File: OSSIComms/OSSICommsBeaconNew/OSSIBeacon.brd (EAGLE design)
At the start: 82 x 82 mm, 21 parts, among them U10 MAX6369, U12 TPS73233, U3 MAX890L, U4 OPA2347, U7 TPS3838, X2 DF13-10PA

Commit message: OSSI New Beacon Board Circuit 90% done
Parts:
- added C10, C11, C14, C15, C16, C22, C25, C32, C4, C5, C6, C8, C9: (no value), OSSI:C0603(1608)
- added C17, C18: 12.5pF, OSSI:C0603(1608)
- added C2, C24, C29, C31: 100nF, OSSI:C0603(1608)
- added C23: 1uF, OSSI:C0603(1608)
- added C26: 1uF,0805, OSSI:C0805(2012)
- added C27, C28, C76: 10nF, OSSI:C0603(1608)
- added C3: 1uF, 0805, OSSI:C0805(2012)
- added C30: 10uF,1210, OSSI:C1210-GCM32
- added C62: 22nF, OSSI:C0603(1608)
- added C7: 1uF 0805, OSSI:C0805(2012)
- added C77: 22pF, OSSI:C0603(1608)
- added F1: LFCN-160, OSSI:LFCN
- added L1, L2: 470nH, 1008 size, OSSI:L1008(2520)
- added L10: 10nH, OSSI:L0603(1608)
- added L3, L4: (no value), OSSI:L0603(1608)
- added LED1: (no value), SparkFun:LED-0603
- added Q2: NX-3215, OSSI:NX-3215
- added R1, R12, R34: 100k, OSSI:R0603(1608)
- added R13: 1.6k, OSSI:R0603(1608)
- added R16: 4.7k, OSSI:R0603(1608)
- added R2, R3: (no value), OSSI:R0603(1608)
- added R25: 3.6k, OSSI:R0603(1608)
- added R33: 1k, OSSI:R0603(1608)
- added R4: 0, OSSI:R0603(1608)
- added R63, R67: 250, OSSI:R0603(1608)
- added R68, R71: 10k, OSSI:R0603(1608)
- added TCXO1: 19.2MHz, OSSI:TCXO_M532
- added TR3: FDV301N, OSSI:SOT23
- added U1: MSP430F2132, OSSI:PW28
- added U2: ADF7012, OSSI:TSSOP24
- added U5: ADL5530, OSSI:LFCSP8_CP
- added U6: MAX890L, OSSI:SO8
- added X1: RFCON-MCX-R/A, OSSI:MCX-R/A
- added X5: JTAG10PINMINI-H, OSSI:M50-3200545
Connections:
- new net BEACON_CE: U1.18, U2.14
- new net BEACON_DATA: U1.24, U2.4
- new net BEACON_MUXOUT: U1.22, U2.6
- new net BEACON_RFOUT: C25.2, C27.1, L4.2
- new net BEACON_SCLK: U1.21, U2.11
- new net BEACON_SDATA: U1.20, U2.12
- new net BEACON_SLE: U1.19, U2.13
- new net BEACON_TCXO: C77.2, U2.8
- new net BEACON_TXCLK: U1.23, U2.5
- new net N$1: R33.1, U1.14
- new net N$10: R67.2, U1.13
- new net N$11: R22.1
- new net N$12: U1.10, U10.1
- new net N$13: U1.11
- new net N$14: L10.1, U2.16
- new net N$15: L10.2, U2.15
- new net N$16: C62.1, C7.2, U2.24
- new net N$17: C62.2, U2.17
- new net N$18: R25.2, U2.23
- new net N$19: C23.1, R12.1, TR3.3, U6.3
- new net N$2: U1.27, X5.3
- new net N$20: C5.1, R3.1
- new net N$21: R13.2, U6.5
- new net N$23: C15.2, L1.P$2, U2.20
- new net N$24: C4.1, R2.1, U2.18
- new net N$25: C3.2, U2.2
- new net N$26: C5.2, C6.2, R2.2, U2.3
- new net N$27: C8.1, C9.1, L1.P$1, R4.2, U2.21
- new net N$28: C27.2, U5.2
- new net N$29: C15.1, C16.2, L3.1
- new net N$3: U1.26, X5.5
- new net N$30: C28.1, L2.P$2, U5.7
- new net N$31: R16.1, X5.10
- new net N$34: C28.2, F1.1
- new net N$35: C32.1, F1.3
- new net N$36: C22.2, L3.2, L4.1
- new net N$37: C32.2, X1.1
- new net N$4: U1.25, X5.7
- new net N$5: C17.1, Q2.2, U1.5
- new net N$6: C18.1, Q2.1, U1.6
- new net N$69: C77.1, TCXO1.3
- new net N$7: LED1.A, R33.2
- new net N$8: U1.28, X5.1
- new net N$9: R63.2, U1.12
- new net PA_-FAULT: R34.1, U1.3, U6.8
- new net PA_ON: R1.2, TR3.1, U1.17
- new net RXD: U1.16
- new net TXD: U1.15
- new net VCCRF: C10.1, C11.1, C14.1, C76.1, R4.1, TCXO1.4, U2.1
- net 3.3VBEACON: now also C2.1, R34.2, R68.2, R71.2, U1.2, X5.4
- net ADC0: now also U1.8
- net ADC1: now also U1.9
- net GND: now also C10.2, C11.2, C14.2, C16.1, C17.2, C18.2, C2.2, C22.1, C23.2, C24.2, C25.1, C26.2, C29.2, C3.1, C30.P$2, C31.2, C4.2, C6.1, C7.1, C76.2, C8.2, C9.2, F1.2, F1.4, LED1.C, R1.1, R13.1, R25.1, R3.2, TCXO1.1, TCXO1.2, TR3.2, U1.4, U2.19, U2.22, U2.7, U5.1, U5.3, U5.4, U5.5, U5.6, U5.8, U6.4, X1.2, X1.3, X1.4, X1.5, X5.9
- net I2CSEC_SCL: now also R67.1, R71.1
- net I2CSEC_SDA: now also R63.1, R68.1
- net RESETBEACON: now also R16.2, U1.7
- net VBEACON_PA: now also C24.1, C26.1, C29.1, C30.P$1, C31.1, L2.P$1, U6.6, U6.7; no longer R22.1
- net VBUS: now also R12.2, U6.1, U6.2

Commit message: New Beacon board updating
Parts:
- added H1, H2, H3, H4: MOUNT-PAD-ROUND3.2, OSSI:3.2-PAD-ROUND
- moved C32 495.0 mm to (67.6, 66.4)
- moved C31 485.7 mm to (55.9, 73.7)
- moved F1 483.7 mm to (62.5, 66.4)
- moved C29 476.8 mm to (55.9, 71.1)
- moved C28 466.1 mm to (58.1, 66.4)
- moved C27 458.6 mm to (47.6, 66.4)
- moved C25 451.8 mm to (45.7, 63.5), turned to 90 degrees
- moved C22 447.7 mm to (43.2, 63.5), turned to 90 degrees
- moved C16 443.7 mm to (40.3, 63.5), turned to 90 degrees
- moved L4 443.1 mm to (44.5, 66.4)
- moved L3 436.5 mm to (41.3, 66.4)
- moved L2 432.3 mm to (54.6, 67.3)
- moved C15 417.2 mm to (37.5, 66.4), turned to 180 degrees
- moved L1 411.2 mm to (33.0, 67.3)
- moved C14 401.8 mm to (26.0, 70.8), turned to 90 degrees
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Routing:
- net 3.3VBEACON: track 0.00 -> 118.2 mm
- net VBEACON_PA: track 0.00 -> 110.7 mm
- net VBUS: track 0.00 -> 72.1 mm
- net BEACON_DATA: track 0.00 -> 60.2 mm
- net BEACON_TXCLK: track 0.00 -> 57.7 mm
- net BEACON_MUXOUT: track 0.00 -> 56.4 mm
- net BEACON_OFF: track 0.00 -> 38.5 mm
- net I2CSEC_SDA: track 0.00 -> 30.1 mm
- net BEACON_-FAULT: track 0.00 -> 30.0 mm
- net BEACON_SCLK: track 0.00 -> 29.6 mm
- net BEACON_SDATA: track 0.00 -> 28.0 mm
- net N$666: track 0.00 -> 26.9 mm
- net I2CSEC_SCL: track 0.00 -> 26.5 mm
- net ADC1: track 0.00 -> 24.0 mm
- net BEACON_WDT_RST: track 0.00 -> 22.7 mm, vias 0 -> 2
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- removed copper zone on layer 1, net GND
- removed copper zone on layer 16, net GND
- removed copper zone on layer 1, net N$34
- removed copper zone on layer 16, net N$34

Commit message: OSSI New Beacon Almost done
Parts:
- added C33, C36: 10pF, OSSI:C0603(1608)
- added C37: 10nF, OSSI:C0603(1608)
- added C38: 100nF, OSSI:C0603(1608)
- added L11: 0 Ohm, OSSI:L0805(2012)
- added Q1: CX5032SB, OSSI:CX5032
- added U$1: OSSILOGORECT, OSSI:OSSILOGORECT1005
- added X3: MOLEX-22-05-7035, OSSI:22-05-7035
- moved X5 74.9 mm to (4.21, 33.7), turned to 270 degrees
- moved R16 63.2 mm to (9.21, 31.1), turned to 0 degrees
- moved R33 58.4 mm to (10.2, 10.6)
- moved LED1 58.3 mm to (10.2, 7.78)
- moved R12 33.8 mm to (39.1, 10.5), turned to 270 degrees
- moved U6 32.8 mm to (34.3, 10.2), turned to 90 degrees
- moved TR3 32.5 mm to (41.9, 12.1)
- moved C24 32.3 mm to (29.2, 11.7), turned to 90 degrees
- moved R1 31.6 mm to (44.8, 12.1)
- moved C23 29.2 mm to (39.1, 13.3), turned to 90 degrees
- moved U10 24.2 mm to (14.0, 32.4), turned to 270 degrees
- moved R13 24.0 mm to (31.8, 14.0), turned to 180 degrees
- moved C1 20.7 mm to (17.1, 32.4), turned to 90 degrees
- moved R34 16.9 mm to (21.6, 38.1), turned to 270 degrees
- moved U1 15.5 mm to (16.5, 41.9), turned to 90 degrees
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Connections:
- removed net I2CSEC_SCL: R67.1, R71.1, X2.4
- removed net I2CSEC_SDA: R63.1, R68.1, X2.5
- removed net N$11: R22.1
- new net BEACON_ADCIN: R22.1, X2.5
- new net BEACON_CWCONTROL: X2.4
- new net N$41: C33.1, Q1.3, U2.9
- net 3.3VBEACON: now also C37.1, L11.1
- net BEACON_SCL: now also R67.1, R71.1
- net BEACON_SDA: now also R63.1, R68.1
- net BEACON_TCXO: now also C36.1, Q1.1
- net GND: now also C33.2, C36.2, C37.2, C38.2, Q1.2, Q1.4, X3.1
- net N$1: now also U1.11; no longer U1.14
- net N$13: now also U1.14; no longer U1.11
- net RXD: now also X3.3
- net TXD: now also X3.2
- net VCCRF: now also C38.1, L11.2
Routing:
- net GND: track 9.76 -> 133.7 mm, vias 0 -> 137
- net VCCRF: track 5.59 -> 112.2 mm, vias 0 -> 2
- net PA_ON: track 10.4 -> 95.4 mm, vias 0 -> 2
- net PA_-FAULT: track 2.53 -> 73.1 mm, vias 0 -> 2
- net TXD: track 0.00 -> 52.6 mm, vias 0 -> 1
- net RXD: track 0.00 -> 51.2 mm, vias 0 -> 1
- net VBEACON_PA: track 110.7 -> 152.5 mm
- net BEACON_ADCIN: track 0.00 -> 39.5 mm, vias 0 -> 2
- net BEACON_SDA: track 0.00 -> 34.2 mm, vias 0 -> 2
- net BEACON_SCL: track 0.00 -> 32.7 mm, vias 0 -> 2
- net I2CSEC_SDA: track 30.1 -> 0.00 mm
- net I2CSEC_SCL: track 26.5 -> 0.00 mm
- net RESETBEACON: track 11.9 -> 36.7 mm, vias 0 -> 2
- net N$666: track 26.9 -> 8.65 mm
- net BEACON_WDT_RST: track 22.7 -> 4.72 mm, vias 2 -> 0
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- added copper zone on layer 1, net GND
- added copper zone on layer 16, net GND
- added copper zone on layer 1, net N$38
- added copper zone on layer 16, net N$38

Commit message: OSSI New Beacon layout done
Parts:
- added C39: 100nF, OSSI:C0603(1608)
- added D1: BAT54S, OSSI:SOT23
- added D2, D3: TPD1E10B06, OSSI:X2SON
- added JP1: (no value), OSSI:JP1
- added R5, R6, R7, R8: 4.7k, OSSI:R0603(1608)
- U8: value TPS73233 -> TPS76933
- moved LED1 39.6 mm to (33.7, 39.7)
- moved R33 39.5 mm to (33.7, 42.4)
- moved C2 4.58 mm to (21.2, 38.6), flipped to the top
- moved Q2 4.43 mm to (24.6, 41.4)
- moved C18 3.55 mm to (27.3, 42.9), turned to 270 degrees
- moved R34 1.80 mm to (22.9, 36.8)
- moved C17 1.21 mm to (27.3, 40.0)
- moved C15 0.48 mm to (37.3, 66.4)
- moved C27 0.48 mm to (47.8, 66.4)
- renumbered U12 to U8
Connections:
- new net N$11: R7.2, U1.16
- new net N$39: R6.2, U1.15
- net 3.3VBEACON: now also D1.2
- net BEACON_ADCIN: now also D3.1
- net BEACON_CWCONTROL: now also D2.1, R5.2, R8.1
- net GND: now also C39.2, D1.1, D2.2, D3.2, JP1.1, R8.2, U8.3
- net N$13: now also C39.1, D1.3, R5.1
- net N$666: no longer U8.3
- net N$7: now also JP1.2
- net RXD: now also R7.1; no longer U1.16
- net TXD: now also R6.1; no longer U1.15
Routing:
- net N$13: track 0.00 -> 37.5 mm
- net GND: track 133.7 -> 98.2 mm, vias 137 -> 163
- net BEACON_CWCONTROL: track 0.00 -> 35.2 mm, vias 0 -> 2
- net PA_-FAULT: track 73.1 -> 61.5 mm
- net 3.3VBEACON: track 103.0 -> 110.2 mm, vias 1 -> 2
- net RXD: track 51.2 -> 57.9 mm
- net N$11: track 0.00 -> 5.15 mm
- net PA_ON: track 95.4 -> 90.3 mm
- net VBEACON_PA: track 152.5 -> 156.7 mm
- net N$7: track 0.00 -> 3.57 mm
- net N$1: track 13.6 -> 17.0 mm
- net N$39: track 0.00 -> 2.97 mm
- net RESETBEACON: track 36.7 -> 34.0 mm
- net N$5: track 10.5 -> 8.34 mm
- net N$6: track 10.5 -> 9.43 mm
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
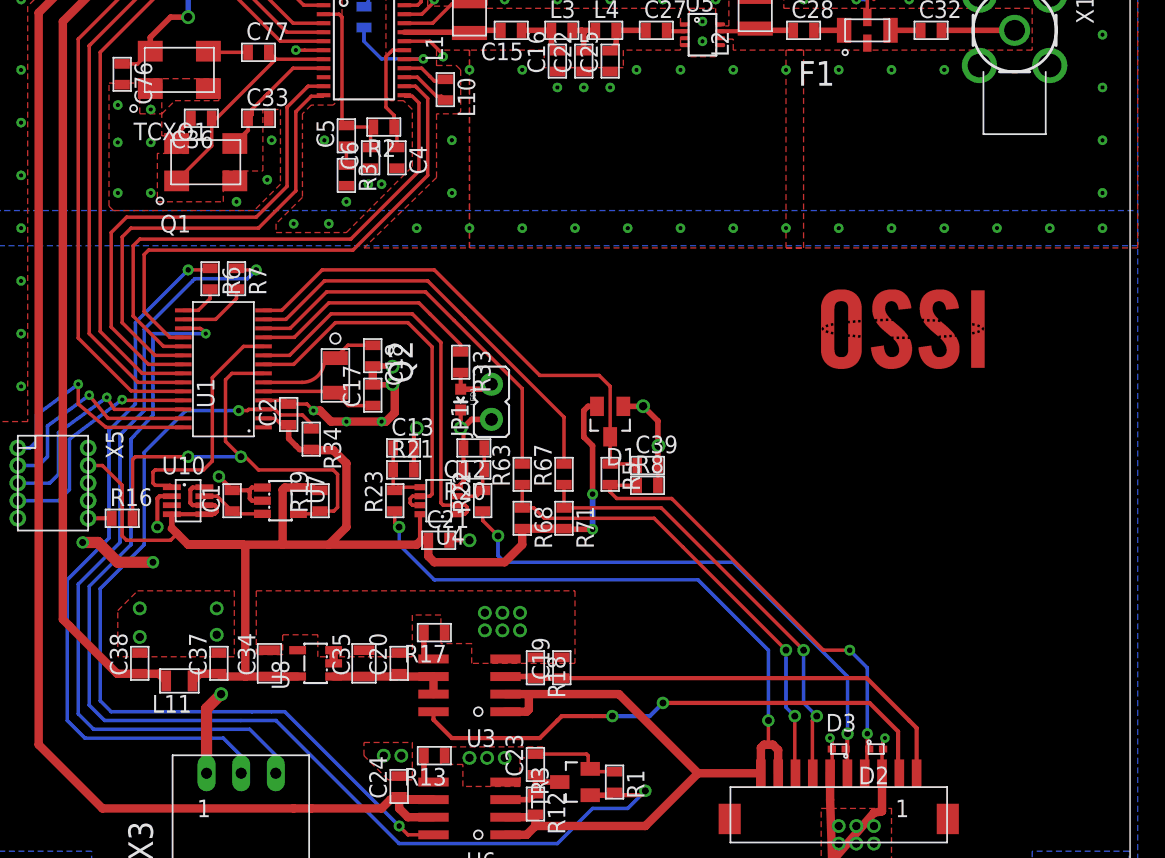
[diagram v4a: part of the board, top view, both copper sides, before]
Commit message: I2C Testboard gerber done / New Beacon gerber done
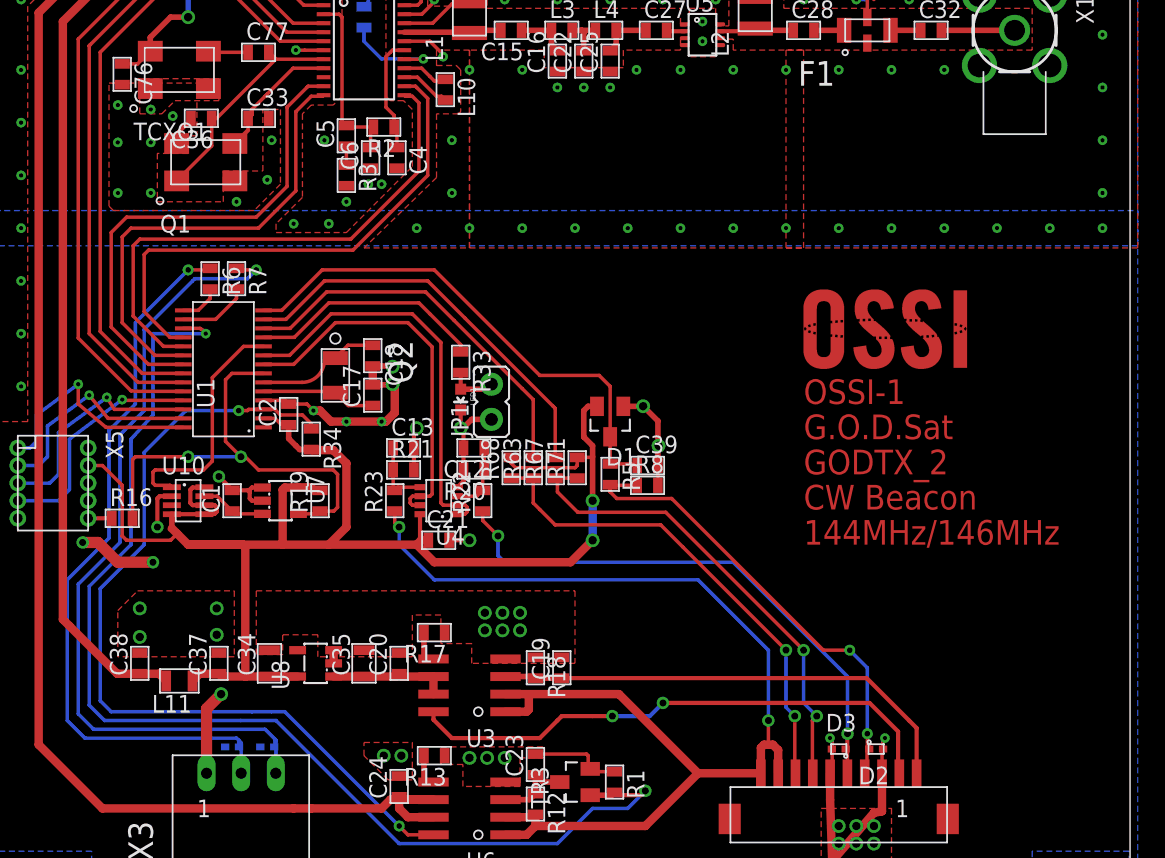
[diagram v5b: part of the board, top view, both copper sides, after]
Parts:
- added D4, D5: TPD1E10B06, OSSI:X2SON
- moved R71 3.77 mm to (42.1, 34.8), turned to 90 degrees
- moved R68 3.74 mm to (37.3, 34.8), turned to 90 degrees
- moved U$1 1.27 mm to (58.4, 41.9)
- moved R63 0.93 mm to (38.9, 34.8)
- moved R67 0.79 mm to (40.5, 34.8)
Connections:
- net GND: now also D4.2, D5.2
- net RXD: now also D5.1
- net TXD: now also D4.1
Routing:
- net 3.3VBEACON: track 110.2 -> 118.0 mm
- net BEACON_SCL: track 32.7 -> 34.6 mm
- net RXD: track 57.9 -> 59.2 mm
- net BEACON_SDA: track 34.2 -> 35.2 mm
- net TXD: track 52.7 -> 53.8 mm
- net N$10: track 30.3 -> 29.6 mm
- net GND: vias 163 -> 164
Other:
- board text added: "144MHz/146MHz"
- board text added: "CW Beacon"
- board text added: "G.O.D.Sat"
- board text added: "GODTX_2"
- board text added: "OSSI-1"
